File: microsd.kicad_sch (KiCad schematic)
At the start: 8 parts, among them J7 503398-1892

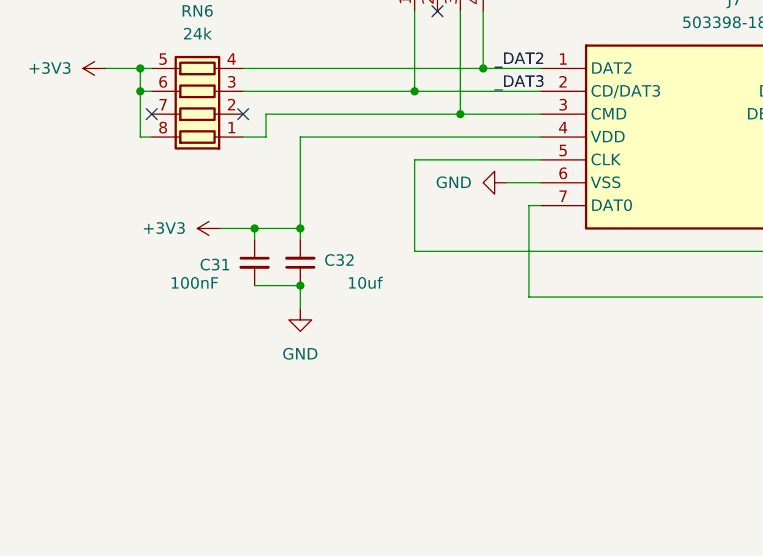
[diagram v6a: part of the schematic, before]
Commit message: 10/01/2025
1v1 fix and v regulator final decision, general BOM corrections and allignments
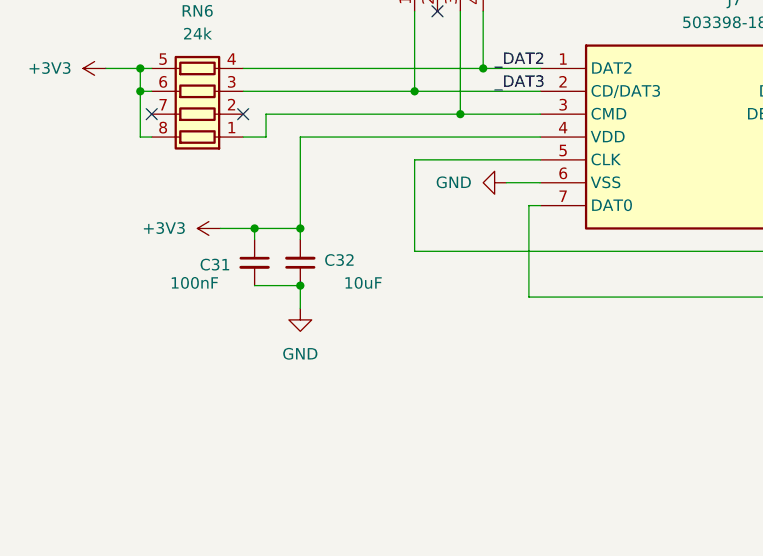
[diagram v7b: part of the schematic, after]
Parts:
- C32: value 10uf -> 10uF
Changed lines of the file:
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@@
 			)
 		)
-		(property "Value" "10uf"
+		(property "Value" "10uF"
 			(at 66.294 69.596 0)
 			(effects
